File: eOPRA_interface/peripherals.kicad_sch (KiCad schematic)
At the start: 23 parts, among them Q7 RU1J002YNTCL, SW1 SW_Push, SW7 Rotary_Encoder_Switch, U4 DS3231MZ+

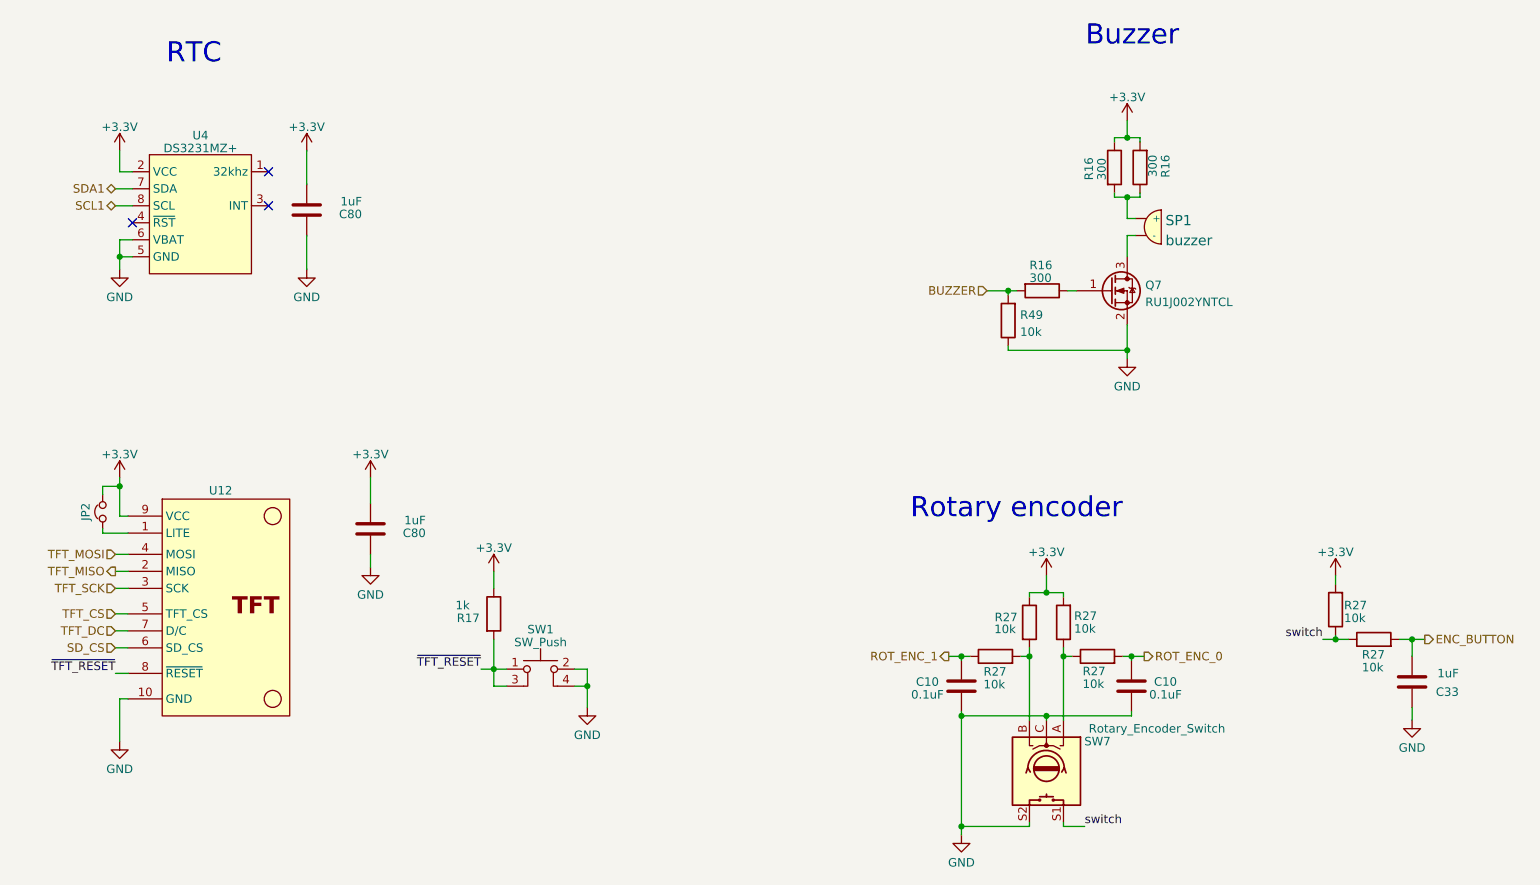
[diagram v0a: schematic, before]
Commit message: switch port on interrupt
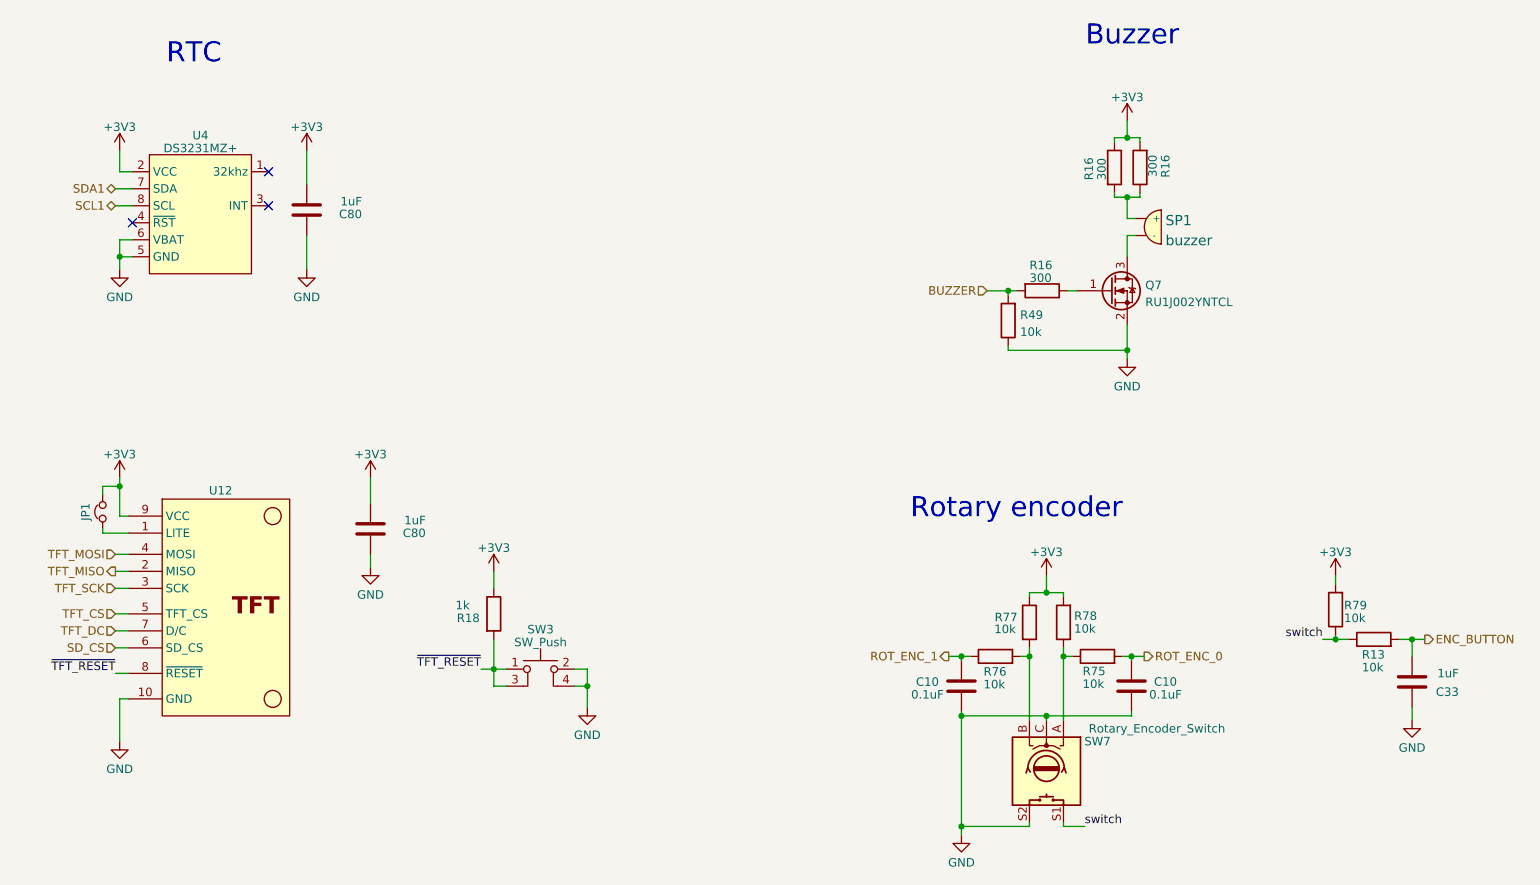
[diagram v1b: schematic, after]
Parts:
- renumbered JP2 to JP1, R27 to R13, R17 to R18, R27 to R75, R27 to R76, R27 to R77, R27 to R78, R27 to R79, SW1 to SW3
